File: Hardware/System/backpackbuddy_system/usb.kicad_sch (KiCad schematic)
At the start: 4 parts

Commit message: labels and stuff almost done
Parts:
- F?: footprint (none) -> Fuse:Fuse_0603_1608Metric_Pad1.05x0.95mm_HandSolder; MPN (none) -> FUSE BRD MNT 0.5A 63VDC 0603; Note (none) -> Not resettable; Stock (none) -> https://www.digikey.com/en/products/detail/bel-fuse-inc/068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
- J?: footprint (none) -> Connector_USB:USB_Micro-B_Molex_47346-0001; Note (none) -> USB_B_Micro; Stock (none) -> https://www.digikey.com/en/products/detail/molex/0473460001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
- R? (x2): footprint (none) -> Resistor_SMD:R_1206_3216Metric_Pad1.30x1.75mm_HandSolder; MPN (none) -> RCC1206 100 22R 1% ET1 E3; Stock (none) -> https://www.digikey.com/en/products/detail/vishay-dale/RCC1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
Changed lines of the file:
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@@
     (property "Reference" "R?" (id 0) (at 163.83 96.52 90))
     (property "Value" "22" (id 1) (at 165.1 93.98 90))
-    (property "Footprint" "" (id 2) (at 165.1 95.758 90)
+    (property "Footprint" "Resistor_SMD:R_1206_3216Metric_Pad1.30x1.75mm_HandSolder" (id 2) (at 165.1 95.758 90)
       (effects (font (size 1.27 1.27)) hide)
     )
     (property "Datasheet" "~" (id 3) (at 165.1 93.98 0)
+      (effects (font (size 1.27 1.27)) hide)
+    )
+    (property "MPN" "RCC1206 100 22R 1% ET1 E3" (id 4) (at 165.1 93.98 0)
+      (effects (font (size 1.27 1.27)) hide)
+    )
+    (property "Stock" "https://www.digikey.com/en/products/detail/vishay-dale/RCC120622R0FKEA/13667242?utm_adgroup=Resistors&utm_source=google&utm_medium=cpc&utm_campaign=Shopping_Supplier_Vishay&utm_term=&utm_content=Resistors" (id 5) (at 165.1 93.98 0)
       (effects (font (size 1.27 1.27)) hide)
     )
@@
     (property "Reference" "J?" (id 0) (at 142.24 78.74 0))
     (property "Value" "USB_B_Micro" (id 1) (at 142.24 81.28 0))
-    (property "Footprint" "" (id 2) (at 146.05 92.71 0)
+    (property "Footprint" "Connector_USB:USB_Micro-B_Molex_47346-0001" (id 2) (at 146.05 92.71 0)
       (effects (font (size 1.27 1.27)) hide)
     )
-    (property "Datasheet" "~" (id 3) (at 146.05 92.71 0)
+    (property "Datasheet" "https://www.molex.com/pdm_docs/sd/473460001_sd.pdf" (id 3) (at 146.05 92.71 0)
+      (effects (font (size 1.27 1.27)) hide)
+    )
+    (property "Note" "USB_B_Micro" (id 4) (at 142.24 91.44 0)
+      (effects (font (size 1.27 1.27)) hide)
+    )
+    (property "Stock" "https://www.digikey.com/en/products/detail/molex/0473460001/1782470" (id 5) (at 142.24 91.44 0)
       (effects (font (size 1.27 1.27)) hide)
     )
@@
     (property "Reference" "F?" (id 0) (at 156.21 80.01 90))
     (property "Value" "500mA" (id 1) (at 156.21 82.55 90))
-    (property "Footprint" "" (id 2) (at 156.21 88.138 90)
+    (property "Footprint" "Fuse:Fuse_0603_1608Metric_Pad1.05x0.95mm_HandSolder" (id 2) (at 156.21 88.138 90)
       (effects (font (size 1.27 1.27)) hide)
     )
     (property "Datasheet" "~" (id 3) (at 156.21 86.36 0)
+      (effects (font (size 1.27 1.27)) hide)
+    )
+    (property "MPN" "FUSE BRD MNT 0.5A 63VDC 0603" (id 4) (at 156.21 86.36 0)
+      (effects (font (size 1.27 1.27)) hide)
+    )
+    (property "Stock" "https://www.digikey.com/en/products/detail/bel-fuse-inc/0686F0500-01/7427694" (id 5) (at 156.21 86.36 0)
+      (effects (font (size 1.27 1.27)) hide)
+    )
+    (property "Note" "Not resettable" (id 6) (at 156.21 86.36 0)
       (effects (font (size 1.27 1.27)) hide)
     )
@@
     (property "Reference" "R?" (id 0) (at 163.83 88.9 90))
     (property "Value" "22" (id 1) (at 165.1 91.44 90))
-    (property "Footprint" "" (id 2) (at 165.1 93.218 90)
+    (property "Footprint" "Resistor_SMD:R_1206_3216Metric_Pad1.30x1.75mm_HandSolder" (id 2) (at 165.1 93.218 90)
       (effects (font (size 1.27 1.27)) hide)
     )
@@
       (effects (font (size 1.27 1.27)) hide)
     )
+    (property "MPN" "RCC1206 100 22R 1% ET1 E3" (id 4) (at 165.1 91.44 0)
+      (effects (font (size 1.27 1.27)) hide)
+    )
+    (property "Stock" "https://www.digikey.com/en/products/detail/vishay-dale/RCC120622R0FKEA/13667242?utm_adgroup=Resistors&utm_source=google&utm_medium=cpc&utm_campaign=Shopping_Supplier_Vishay&utm_term=&utm_content=Resistors" (id 5) (at 165.1 91.44 0)
+      (effects (font (size 1.27 1.27)) hide)
+    )

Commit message: combining both sheets
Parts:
- gave numbers to parts that had none: 4
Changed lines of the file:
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@@
   (symbol (lib_id "Device:R") (at 165.1 93.98 90) (unit 1)
     (in_bom yes) (on_board yes)
-    (property "Reference" "R?" (id 0) (at 163.83 96.52 90))
+    (property "Reference" "R3" (id 0) (at 163.83 96.52 90))
     (property "Value" "22" (id 1) (at 165.1 93.98 90))
     (property "Footprint" "Resistor_SMD:R_1206_3216Metric_Pad1.30x1.75mm_HandSolder" (id 2) (at 165.1 95.758 90)
@@
   (symbol (lib_id "Connector:USB_B_Micro") (at 142.24 91.44 0) (unit 1)
     (in_bom yes) (on_board yes) (fields_autoplaced)
-    (property "Reference" "J?" (id 0) (at 142.24 78.74 0))
+    (property "Reference" "J10" (id 0) (at 142.24 78.74 0))
     (property "Value" "USB_B_Micro" (id 1) (at 142.24 81.28 0))
     (property "Footprint" "Connector_USB:USB_Micro-B_Molex_47346-0001" (id 2) (at 146.05 92.71 0)
@@
   (symbol (lib_id "power:GND") (at 142.24 105.41 0) (unit 1)
     (in_bom yes) (on_board yes) (fields_autoplaced)
-    (property "Reference" "#PWR?" (id 0) (at 142.24 111.76 0)
+    (property "Reference" "#PWR026" (id 0) (at 142.24 111.76 0)
       (effects (font (size 1.27 1.27)) hide)
     )
@@
   (symbol (lib_id "Device:Fuse") (at 156.21 86.36 90) (unit 1)
     (in_bom yes) (on_board yes) (fields_autoplaced)
-    (property "Reference" "F?" (id 0) (at 156.21 80.01 90))
+    (property "Reference" "F1" (id 0) (at 156.21 80.01 90))
     (property "Value" "500mA" (id 1) (at 156.21 82.55 90))
     (property "Footprint" "Fuse:Fuse_0603_1608Metric_Pad1.05x0.95mm_HandSolder" (id 2) (at 156.21 88.138 90)
@@
   (symbol (lib_id "power:+5V") (at 162.56 81.28 0) (unit 1)
     (in_bom yes) (on_board yes) (fields_autoplaced)
-    (property "Reference" "#PWR?" (id 0) (at 162.56 85.09 0)
+    (property "Reference" "#PWR027" (id 0) (at 162.56 85.09 0)
       (effects (font (size 1.27 1.27)) hide)
     )
@@
   (symbol (lib_id "Device:R") (at 165.1 91.44 90) (unit 1)
     (in_bom yes) (on_board yes)
-    (property "Reference" "R?" (id 0) (at 163.83 88.9 90))
+    (property "Reference" "R2" (id 0) (at 163.83 88.9 90))
     (property "Value" "22" (id 1) (at 165.1 91.44 90))
     (property "Footprint" "Resistor_SMD:R_1206_3216Metric_Pad1.30x1.75mm_HandSolder" (id 2) (at 165.1 93.218 90)

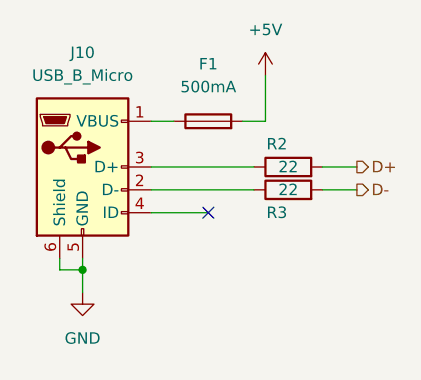
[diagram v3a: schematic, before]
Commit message: schematic mostly done, just need to fix ERC, decoup caps, TP
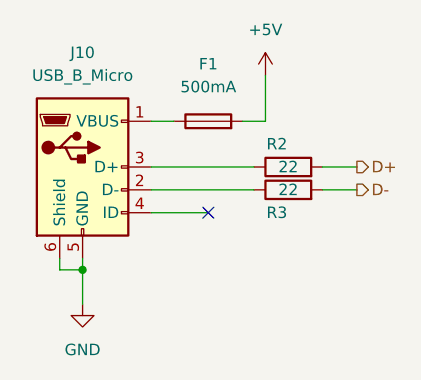
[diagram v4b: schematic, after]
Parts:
- J10: Note USB_B_Micro -> (none)
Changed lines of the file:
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@@
-    (stroke (width 0) (type default) (color 0 0 0 0))
-  )
-  (wire (pts (xy 139.7 102.87) (xy 142.24 102.87))
     (stroke (width 0) (type default) (color 0 0 0 0))
   )
@@
     (stroke (width 0) (type default) (color 0 0 0 0))
   )
-  (wire (pts (xy 142.24 102.87) (xy 142.24 105.41))
+  (wire (pts (xy 142.24 102.87) (xy 142.24 106.68))
+    (stroke (width 0) (type default) (color 0 0 0 0))
+  )
+  (wire (pts (xy 139.7 102.87) (xy 139.7 101.6))
     (stroke (width 0) (type default) (color 0 0 0 0))
   )
@@
     (stroke (width 0) (type default) (color 0 0 0 0))
   )
-  (wire (pts (xy 139.7 101.6) (xy 139.7 102.87))
+  (wire (pts (xy 160.02 86.36) (xy 162.56 86.36))
+    (stroke (width 0) (type default) (color 0 0 0 0))
+  )
+  (wire (pts (xy 142.24 102.87) (xy 139.7 102.87))
     (stroke (width 0) (type default) (color 0 0 0 0))
   )
   (wire (pts (xy 142.24 101.6) (xy 142.24 102.87))
-    (stroke (width 0) (type default) (color 0 0 0 0))
-  )
-  (wire (pts (xy 160.02 86.36) (xy 162.56 86.36))
     (stroke (width 0) (type default) (color 0 0 0 0))
   )
@@
     (pin "2")
   )
-  (symbol (lib_id "Connector:USB_B_Micro") (at 142.24 91.44 0) (unit 1)
-    (in_bom yes) (on_board yes) (fields_autoplaced)
-    (property "Reference" "J10" (id 0) (at 142.24 78.74 0))
-    (property "Value" "USB_B_Micro" (id 1) (at 142.24 81.28 0))
-    (property "Footprint" "Connector_USB:USB_Micro-B_Molex_47346-0001" (id 2) (at 146.05 92.71 0)
-      (effects (font (size 1.27 1.27)) hide)
-    )
-    (property "Datasheet" "https://www.molex.com/pdm_docs/sd/473460001_sd.pdf" (id 3) (at 146.05 92.71 0)
-      (effects (font (size 1.27 1.27)) hide)
-    )
-    (property "Note" "USB_B_Micro" (id 4) (at 142.24 91.44 0)
-      (effects (font (size 1.27 1.27)) hide)
-    )
-    (property "Stock" "https://www.digikey.com/en/products/detail/molex/0473460001/1782470" (id 5) (at 142.24 91.44 0)
-      (effects (font (size 1.27 1.27)) hide)
-    )
-    (pin "1")
-    (pin "2")
-    (pin "3")
-    (pin "4")
-    (pin "5")
-    (pin "6")
-  )
-  (symbol (lib_id "power:GND") (at 142.24 105.41 0) (unit 1)
-    (in_bom yes) (on_board yes) (fields_autoplaced)
-    (property "Reference" "#PWR026" (id 0) (at 142.24 111.76 0)
-      (effects (font (size 1.27 1.27)) hide)
-    )
-    (property "Value" "GND" (id 1) (at 142.24 110.49 0))
-    (property "Footprint" "" (id 2) (at 142.24 105.41 0)
-      (effects (font (size 1.27 1.27)) hide)
-    )
-    (property "Datasheet" "" (id 3) (at 142.24 105.41 0)
-      (effects (font (size 1.27 1.27)) hide)
-    )
-    (pin "1")
-  )
   (symbol (lib_id "Device:Fuse") (at 156.21 86.36 90) (unit 1)
     (in_bom yes) (on_board yes) (fields_autoplaced)
@@
     (pin "1")
     (pin "2")
+  )
+  (symbol (lib_id "power:GND") (at 142.24 106.68 0) (unit 1)
+    (in_bom yes) (on_board yes) (fields_autoplaced)
+    (property "Reference" "#PWR0105" (id 0) (at 142.24 113.03 0)
+      (effects (font (size 1.27 1.27)) hide)
+    )
+    (property "Value" "GND" (id 1) (at 142.24 111.76 0))
+    (property "Footprint" "" (id 2) (at 142.24 106.68 0)
+      (effects (font (size 1.27 1.27)) hide)
+    )
+    (property "Datasheet" "" (id 3) (at 142.24 106.68 0)
+      (effects (font (size 1.27 1.27)) hide)
+    )
+    (pin "1")
   )
   (symbol (lib_id "power:+5V") (at 162.56 81.28 0) (unit 1)
@@
     (pin "2")
   )
+  (symbol (lib_id "Connector:USB_B_Micro") (at 142.24 91.44 0) (unit 1)
+    (in_bom yes) (on_board yes) (fields_autoplaced)
+    (property "Reference" "J10" (id 0) (at 142.24 78.74 0))
+    (property "Value" "USB_B_Micro" (id 1) (at 142.24 81.28 0))
+    (property "Footprint" "Connector_USB:USB_Micro-B_Molex_47346-0001" (id 2) (at 146.05 92.71 0)
+      (effects (font (size 1.27 1.27)) hide)
+    )
+    (property "Datasheet" "https://www.molex.com/pdm_docs/sd/473460001_sd.pdf" (id 3) (at 146.05 92.71 0)
+      (effects (font (size 1.27 1.27)) hide)
+    )
+    (property "Stock" "https://www.digikey.com/en/products/detail/molex/0473460001/1782470" (id 4) (at 142.24 91.44 0)
+      (effects (font (size 1.27 1.27)) hide)
+    )
+    (pin "1")
+    (pin "2")
+    (pin "3")
+    (pin "4")
+    (pin "5")
+    (pin "6")
+  )
 )
